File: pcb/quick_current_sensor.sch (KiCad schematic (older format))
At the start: 24 parts, among them J1 +Vcc, J2 GND, J3 +LOAD, J4 -LOAD, J5 Vout, J6 GND, Q1 MTP2P50E, U1 LM358N, U2 TL431LP

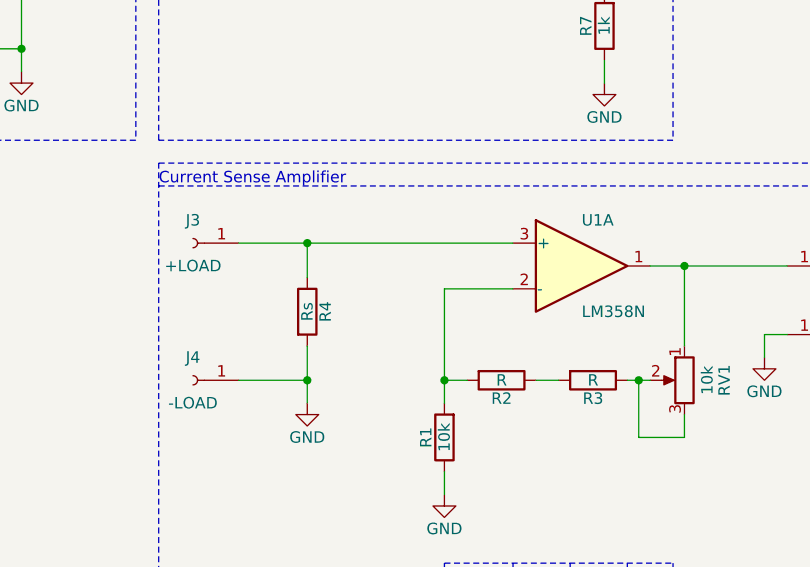
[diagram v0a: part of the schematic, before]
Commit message: add Rs footprint and 3d model
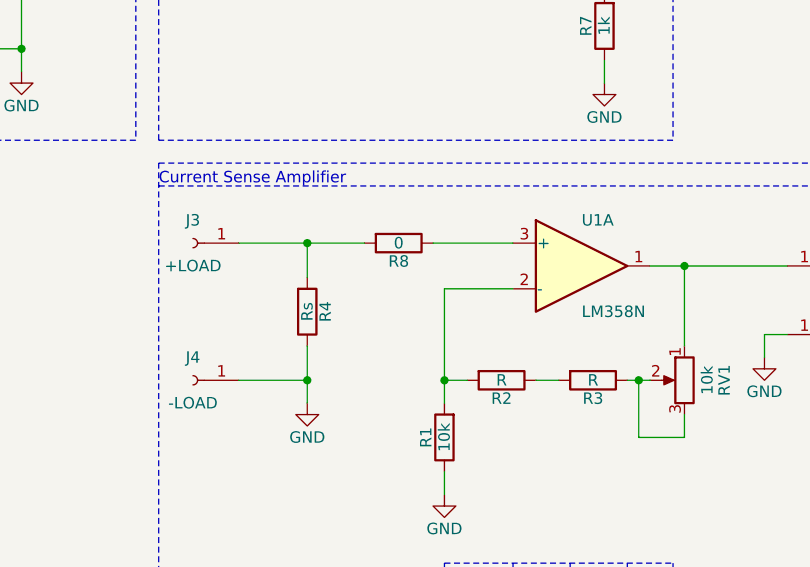
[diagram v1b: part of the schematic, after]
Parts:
- added R8: 0, Resistor_THT:R_Axial_DIN0207_L6.3mm_D2.5mm_P10.16mm_Horizontal, symbol Device:R
- R4: footprint (none) -> pl_DalePR:RH-10
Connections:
- net GND: now also R4.1; no longer R4.2
- new net: R8.1, U1.3 (+)
- new net: J3.1 (Pin_1), R4.2, R8.2
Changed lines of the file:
@@
 F 0 "R4" V 3980 3400 50  0000 C CNN
 F 1 "Rs" V 3900 3400 50  0000 C CNN
-F 2 "" V 3830 3400 50  0001 C CNN
+F 2 "pl_DalePR:RH-10" V 3830 3400 50  0001 C CNN
 F 3 "~" H 3900 3400 50  0001 C CNN
 	1    3900 3400
-	1    0    0    -1
+	1    0    0    1
 $EndComp
 $Comp
@@
 Wire Wire Line
 	3900 3100 3900 3250
-Wire Wire Line
-	3900 3100 4800 3100
-Connection ~ 3900 3100
 Wire Wire Line
 	5400 3200 5550 3200
@@
 	1    0    0    -1
 $EndComp
+$Comp
+L Device:R R8
+U 1 1 5FFF27F8
+P 4300 3100
+F 0 "R8" V 4380 3100 50  0000 C CNN
+F 1 "0" V 4300 3100 50  0000 C CNN
+F 2 "Resistor_THT:R_Axial_DIN0207_L6.3mm_D2.5mm_P10.16mm_Horizontal" V 4230 3100 50  0001 C CNN
+F 3 "~" H 4300 3100 50  0001 C CNN
+	1    4300 3100
+	0    1    1    0
+$EndComp
+Wire Wire Line
+	4450 3100 4800 3100
+Wire Wire Line
+	4150 3100 3900 3100
+Connection ~ 3900 3100
 $EndSCHEMATC

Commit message: cleanup and add logo
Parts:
- U2: footprint Package_TO_SOT_THT:TO-92_Inline -> Package_TO_SOT_THT:TO-92_W4.0mm_StaggerEven_Horizontal_FlatSideDown
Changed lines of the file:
@@
 F 0 "U2" H 3400 1700 50  0000 C CNN
 F 1 "TL431LP" H 3500 1500 50  0000 C CNN
-F 2 "Package_TO_SOT_THT:TO-92_Inline" H 3500 1450 50  0001 C CIN
+F 2 "Package_TO_SOT_THT:TO-92_W4.0mm_StaggerEven_Horizontal_FlatSideDown" H 3500 1450 50  0001 C CIN
 F 3 "http://www.ti.com/lit/ds/symlink/tl431.pdf" H 3500 1600 50  0001 C CIN
 	1    3500 1600

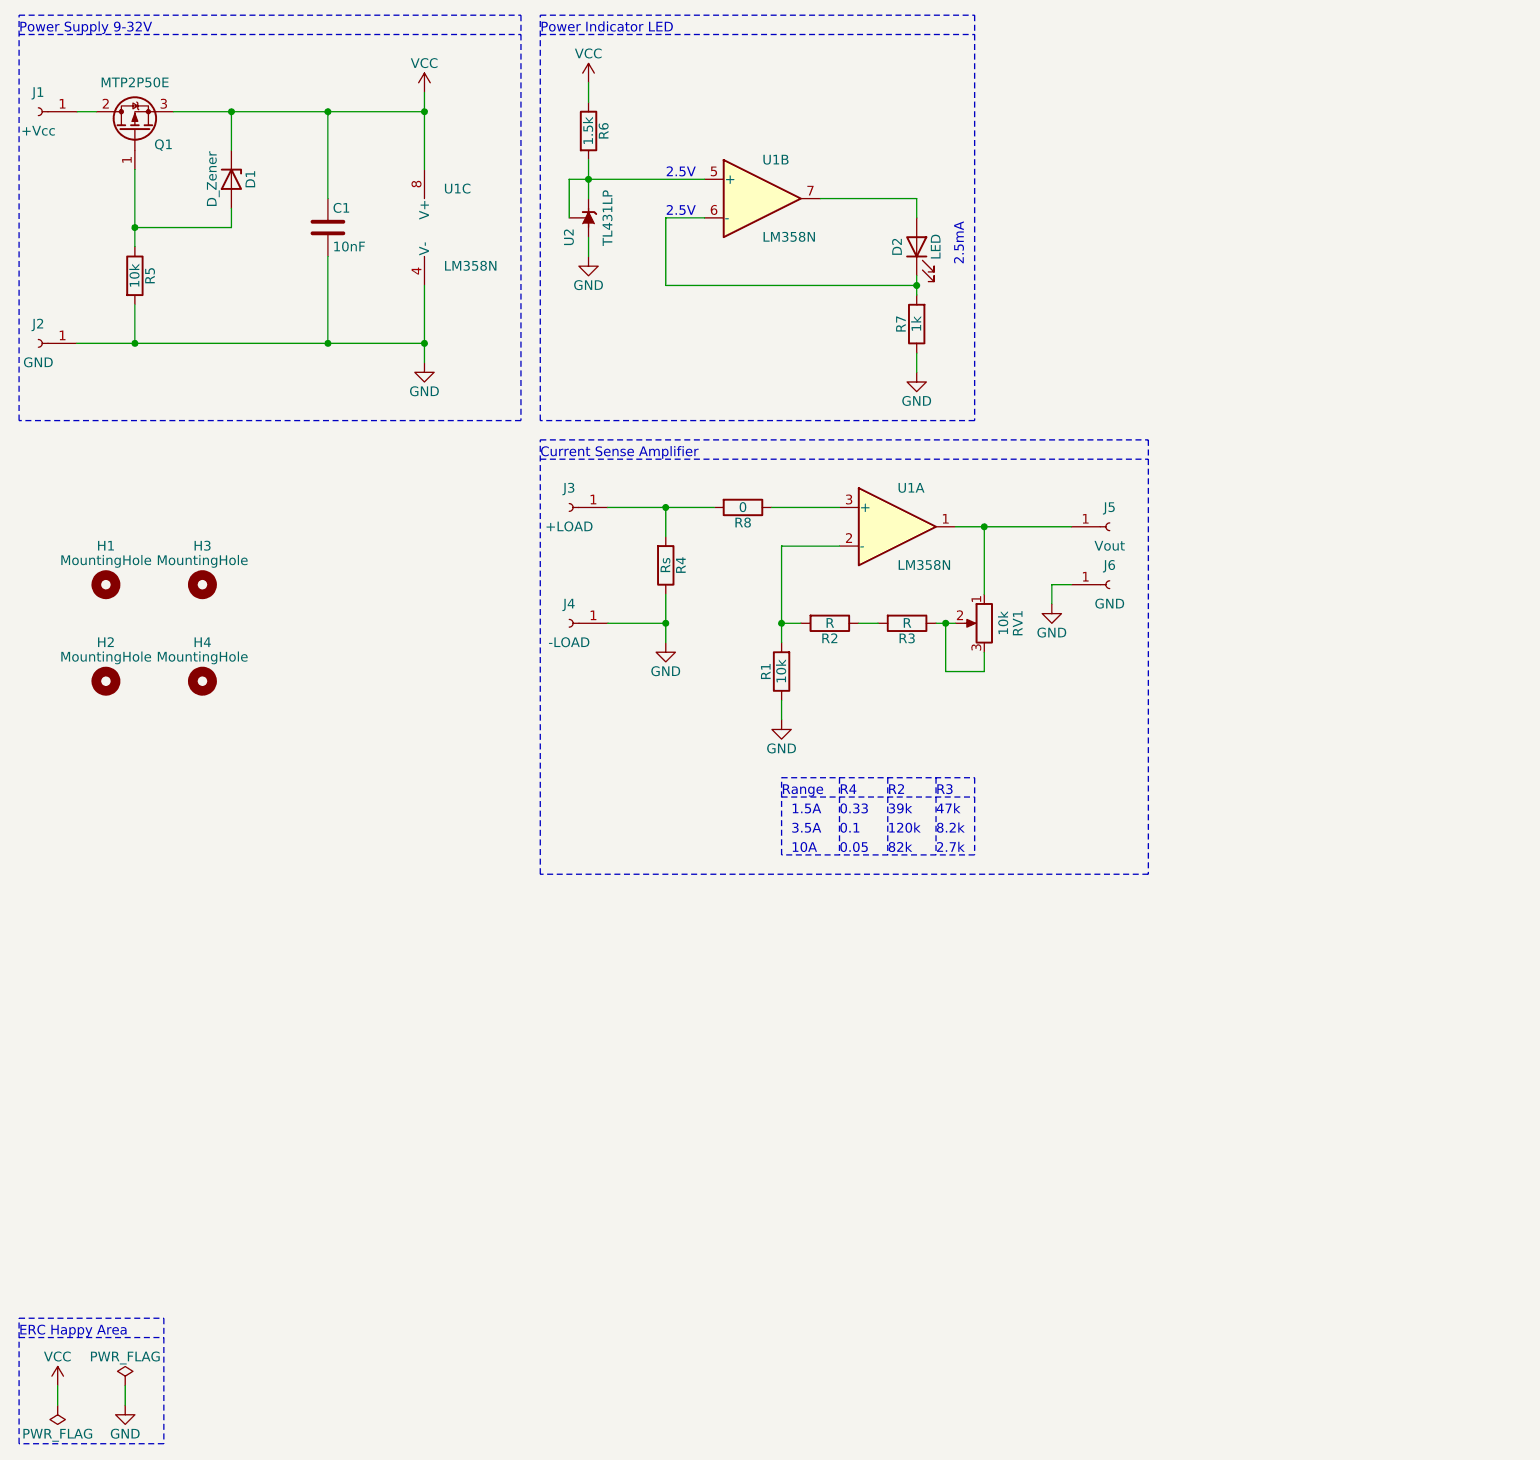
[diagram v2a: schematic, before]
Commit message: change power and vout to terminal blocks
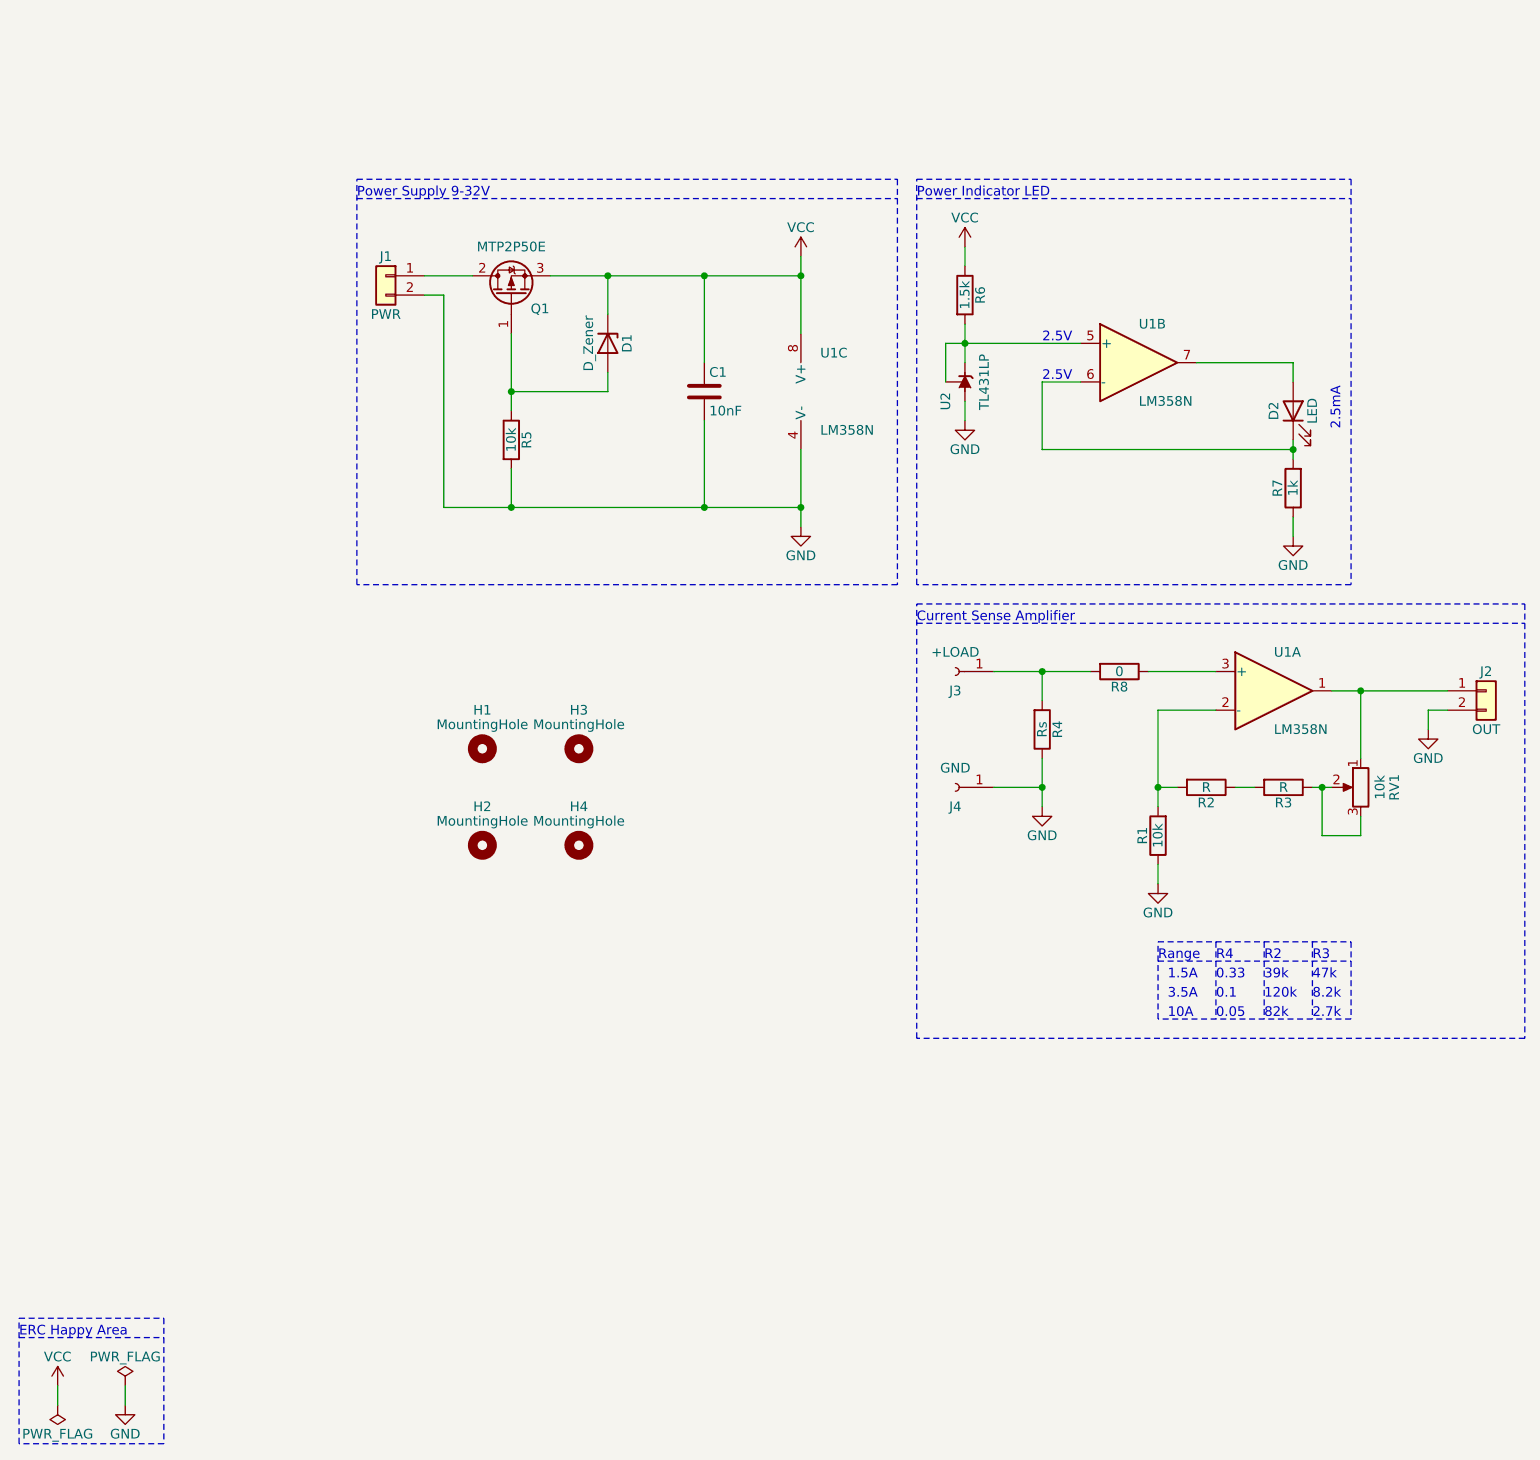
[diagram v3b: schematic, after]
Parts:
- removed J1: +Vcc, pl_Banana:banana_edge_mount, symbol Connector:Conn_01x01_Female
- removed J2, J6: GND, pl_Banana:banana_edge_mount, symbol Connector:Conn_01x01_Female
- removed J5: Vout, pl_Banana:banana_edge_mount, symbol Connector:Conn_01x01_Female
- added J1: PWR, pl_TerminalBlock:WJ127-5.0-2P, symbol Connector_Generic:Conn_01x02
- added J2: OUT, pl_TerminalBlock:WJ127-5.0-2P, symbol Connector_Generic:Conn_01x02
- J4: value -LOAD -> GND
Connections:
- net GND: now also J1.2 (Pin_2), J2.2 (Pin_2)
- net at RV1.1, U1.1: now also J2.1 (Pin_1)
- net at Q1.2 (D): now also J1.1 (Pin_1)
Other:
- moved on the sheet: C1, D1, D2, H1, H2, H3, H4, Q1, R1, R2, R3, R4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

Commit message: cleanup, reduce size
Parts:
- removed H1, H2, H3, H4: MountingHole, MountingHole:MountingHole_3.2mm_M3, symbol Mechanical:MountingHole
- removed R8: 0, Resistor_THT:R_Axial_DIN0207_L6.3mm_D2.5mm_P10.16mm_Horizontal, symbol Device:R
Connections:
- net at U1.3 (+): now also J3.1 (Pin_1), R4.2
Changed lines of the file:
@@
 Wire Wire Line
 	7300 4550 7350 4550
-$Comp
-L Mechanical:MountingHole H1
-U 1 1 6022130F
-P 2950 4350
-F 0 "H1" H 2950 4550 50  0000 C CNN
-F 1 "MountingHole" H 2950 4475 50  0000 C CNN
-F 2 "MountingHole:MountingHole_3.2mm_M3" H 2950 4350 50  0001 C CNN
-F 3 "~" H 2950 4350 50  0001 C CNN
-	1    2950 4350
-	1    0    0    -1
-$EndComp
-$Comp
-L Mechanical:MountingHole H3
-U 1 1 60221DA9
-P 3450 4350
-F 0 "H3" H 3450 4550 50  0000 C CNN
-F 1 "MountingHole" H 3450 4475 50  0000 C CNN
-F 2 "MountingHole:MountingHole_3.2mm_M3" H 3450 4350 50  0001 C CNN
-F 3 "~" H 3450 4350 50  0001 C CNN
-	1    3450 4350
-	1    0    0    -1
-$EndComp
-$Comp
-L Mechanical:MountingHole H2
-U 1 1 602225A1
-P 2950 4850
-F 0 "H2" H 2950 5050 50  0000 C CNN
-F 1 "MountingHole" H 2950 4975 50  0000 C CNN
-F 2 "MountingHole:MountingHole_3.2mm_M3" H 2950 4850 50  0001 C CNN
-F 3 "~" H 2950 4850 50  0001 C CNN
-	1    2950 4850
-	1    0    0    -1
-$EndComp
-$Comp
-L Mechanical:MountingHole H4
-U 1 1 60222CEF
-P 3450 4850
-F 0 "H4" H 3450 5050 50  0000 C CNN
-F 1 "MountingHole" H 3450 4975 50  0000 C CNN
-F 2 "MountingHole:MountingHole_3.2mm_M3" H 3450 4850 50  0001 C CNN
-F 3 "~" H 3450 4850 50  0001 C CNN
-	1    3450 4850
-	1    0    0    -1
-$EndComp
-$Comp
-L Device:R R8
-U 1 1 5FFF27F8
-P 6250 3950
-F 0 "R8" V 6330 3950 50  0000 C CNN
-F 1 "0" V 6250 3950 50  0000 C CNN
-F 2 "Resistor_THT:R_Axial_DIN0207_L6.3mm_D2.5mm_P10.16mm_Horizontal" V 6180 3950 50  0001 C CNN
-F 3 "~" H 6250 3950 50  0001 C CNN
-	1    6250 3950
-	0    1    1    0
-$EndComp
-Wire Wire Line
-	6400 3950 6750 3950
-Wire Wire Line
-	6100 3950 5850 3950
 Connection ~ 5850 3950
-$Comp
-L Connector_Generic:Conn_01x02 J1
-U 1 1 60018C46
-P 2450 1900
-F 0 "J1" H 2450 2000 50  0000 C CNN
-F 1 "PWR" H 2450 1700 50  0000 C CNN
-F 2 "pl_TerminalBlock:WJ127-5.0-2P" H 2450 1900 50  0001 C CNN
-F 3 "~" H 2450 1900 50  0001 C CNN
-	1    2450 1900
-	-1   0    0    -1
-$EndComp
 Wire Wire Line
 	2650 2000 2750 2000
@@
 	-1   0    0    1
 $EndComp
+$Comp
+L Connector_Generic:Conn_01x02 J1
+U 1 1 60018C46
+P 2450 1900
+F 0 "J1" H 2450 2000 50  0000 C CNN
+F 1 "PWR" H 2450 1700 50  0000 C CNN
+F 2 "pl_TerminalBlock:WJ127-5.0-2P" H 2450 1900 50  0001 C CNN
+F 3 "~" H 2450 1900 50  0001 C CNN
+	1    2450 1900
+	-1   0    0    -1
+$EndComp
+Wire Wire Line
+	5850 3950 6750 3950
 $EndSCHEMATC
